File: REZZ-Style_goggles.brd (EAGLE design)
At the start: 65.5 x 65.5 mm, 85 parts

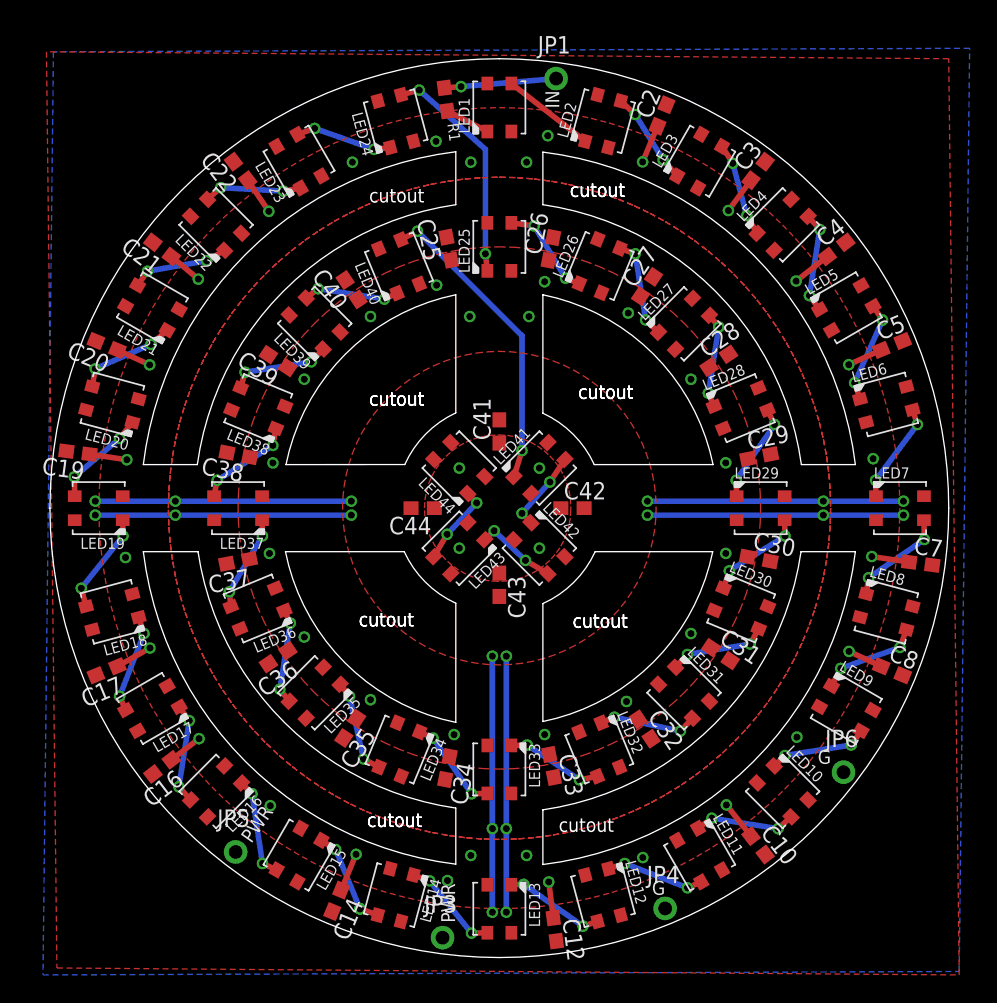
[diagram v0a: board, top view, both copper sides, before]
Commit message: revised pads, adjusted silk screen
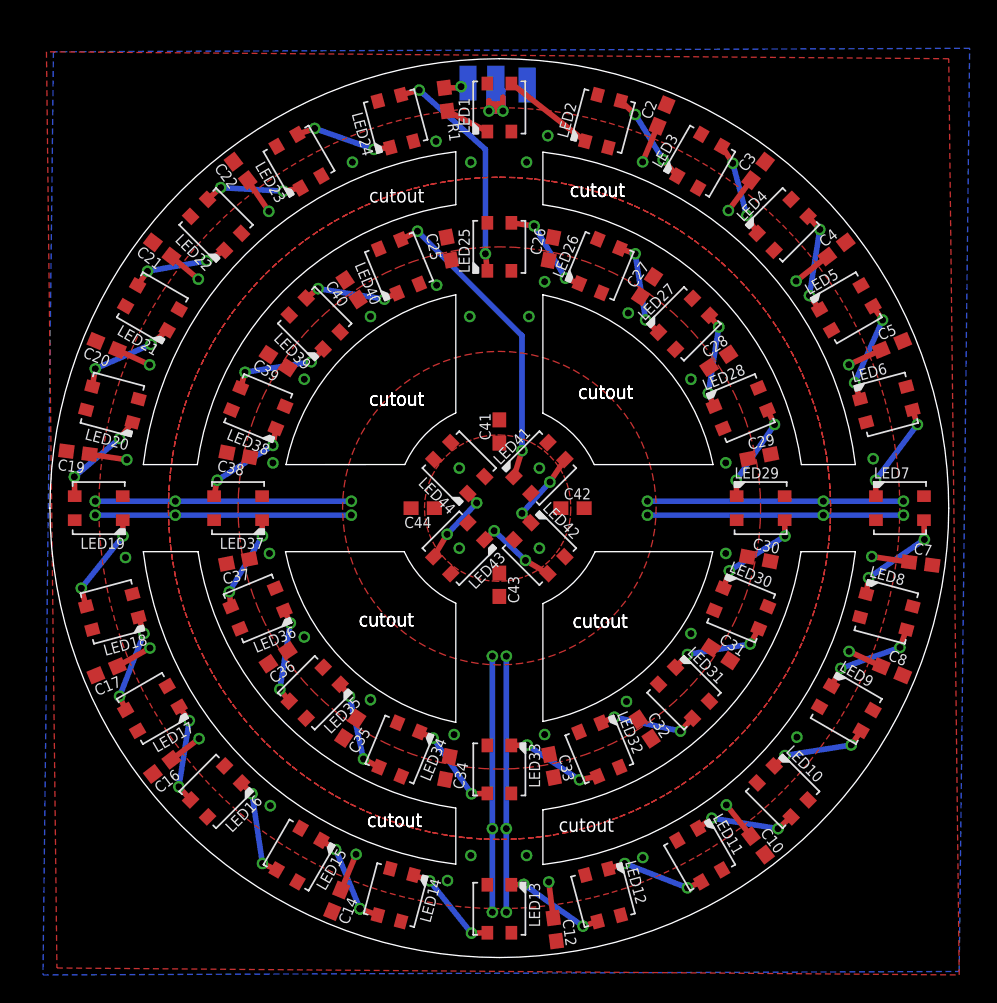
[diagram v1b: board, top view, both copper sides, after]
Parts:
- removed JP1, JP3, JP4, JP5, JP6: (no value), NeoPixelRing:1X01-CLEANBIG
- added GND, INPUT, VDD: WIREPADSMD1,27-254, wirepad:SMD1,27-2,54
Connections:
- net GND: now also GND.1; no longer JP4.1, JP6.1
- net N$26: now also INPUT.1; no longer JP1.1
- net VDD: now also VDD.1; no longer JP3.1, JP5.1
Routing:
- net GND: track 112.0 -> 125.2 mm, vias 18 -> 20
- net N$26: track 8.18 -> 2.07 mm
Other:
- board text removed: "Data Input"
- board text removed: "G"
- board text removed: "GND"
- board text removed: "IN"
- board text removed: "PWR"
- board text removed: "PWR +5V"
